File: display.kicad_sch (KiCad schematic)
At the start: 10 parts

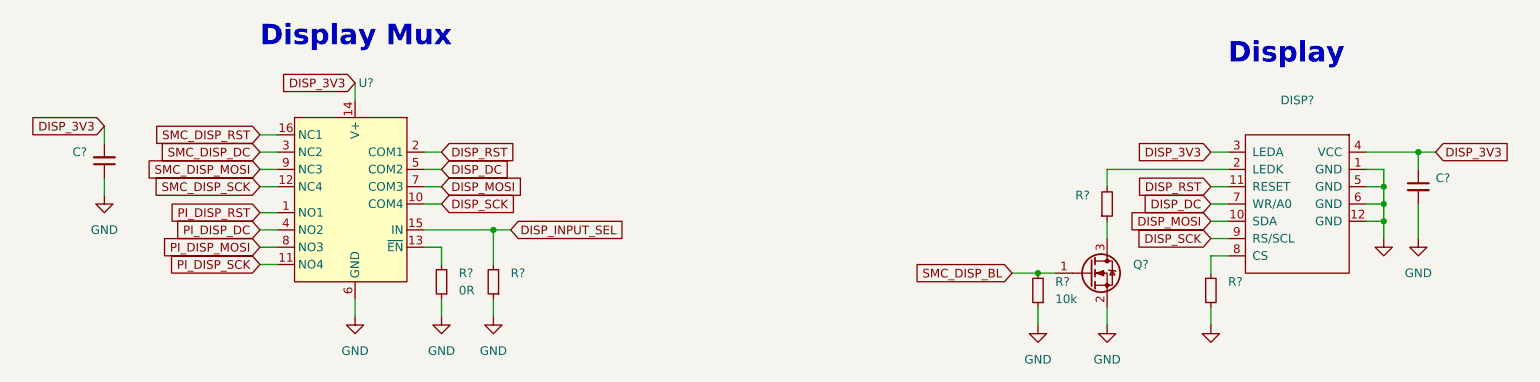
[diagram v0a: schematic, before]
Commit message: schem: first pass done, ERC passing
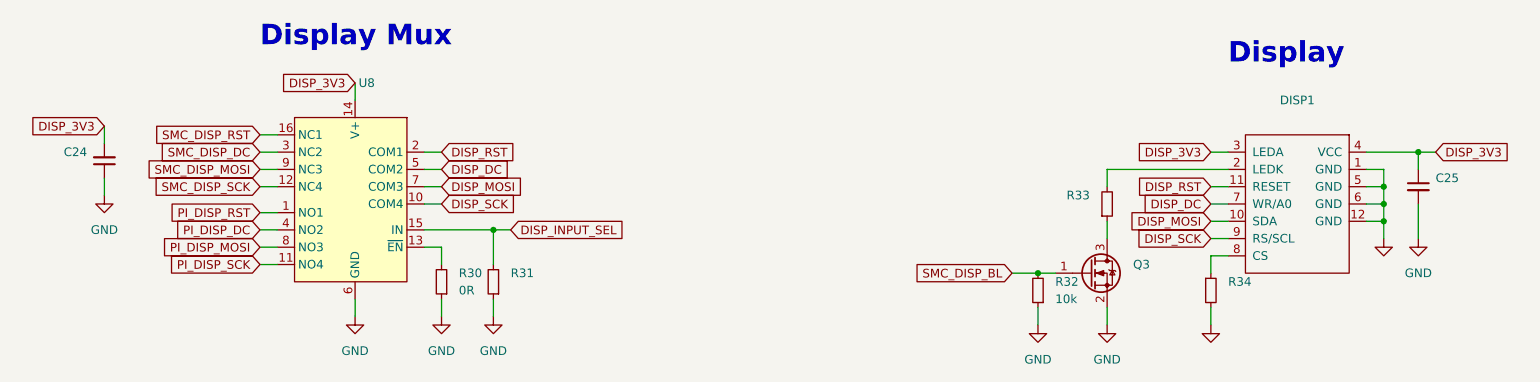
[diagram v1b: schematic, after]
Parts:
- Q3: renamed from Q?; footprint (none) -> Package_TO_SOT_SMD:SOT-23
- U8: renamed from U?; footprint (none) -> lcsc:UQFN-16_L2.6-W1.8-P0.40-BL
- gave numbers to parts that had none: 8
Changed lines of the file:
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@@
   (symbol (lib_id "lcsc:TS3A5018RSVR") (at 81.28 111.76 0) (mirror y) (unit 1)
     (in_bom yes) (on_board yes) (fields_autoplaced)
-    (property "Reference" "U?" (id 0) (at 81.8006 93.98 0)
+    (property "Reference" "U8" (id 0) (at 81.8006 93.98 0)
       (effects (font (size 1.27 1.27)) (justify right))
     )
@@
       (effects (font (size 1.27 1.27)) (justify right))
     )
-    (property "Footprint" "" (id 2) (at 81.28 135.89 0)
+    (property "Footprint" "lcsc:UQFN-16_L2.6-W1.8-P0.40-BL" (id 2) (at 81.28 135.89 0)
       (effects (font (size 1.27 1.27)) hide)
     )
@@
   (symbol (lib_id "power:GND") (at 237.49 116.84 0) (unit 1)
     (in_bom yes) (on_board yes) (fields_autoplaced)
-    (property "Reference" "#PWR?" (id 0) (at 237.49 123.19 0)
+    (property "Reference" "#PWR077" (id 0) (at 237.49 123.19 0)
       (effects (font (size 1.27 1.27)) hide)
     )
@@
   (symbol (lib_id "power:GND") (at 81.28 128.27 0) (unit 1)
     (in_bom yes) (on_board yes) (fields_autoplaced)
-    (property "Reference" "#PWR?" (id 0) (at 81.28 134.62 0)
+    (property "Reference" "#PWR070" (id 0) (at 81.28 134.62 0)
       (effects (font (size 1.27 1.27)) hide)
     )
@@
   (symbol (lib_id "Device:R_Small") (at 191.77 111.76 0) (mirror x) (unit 1)
     (in_bom yes) (on_board yes) (fields_autoplaced)
-    (property "Reference" "R?" (id 0) (at 189.23 110.4899 0)
+    (property "Reference" "R33" (id 0) (at 189.23 110.4899 0)
       (effects (font (size 1.27 1.27)) (justify right))
     )
@@
   (symbol (lib_id "Device:R_Small") (at 101.6 123.19 180) (unit 1)
     (in_bom yes) (on_board yes) (fields_autoplaced)
-    (property "Reference" "R?" (id 0) (at 104.14 121.9199 0)
+    (property "Reference" "R31" (id 0) (at 104.14 121.9199 0)
       (effects (font (size 1.27 1.27)) (justify right))
     )
@@
   (symbol (lib_id "power:GND") (at 191.77 129.54 0) (unit 1)
     (in_bom yes) (on_board yes) (fields_autoplaced)
-    (property "Reference" "#PWR?" (id 0) (at 191.77 135.89 0)
+    (property "Reference" "#PWR074" (id 0) (at 191.77 135.89 0)
       (effects (font (size 1.27 1.27)) hide)
     )
@@
   (symbol (lib_id "power:GND") (at 232.41 116.84 0) (unit 1)
     (in_bom yes) (on_board yes) (fields_autoplaced)
-    (property "Reference" "#PWR?" (id 0) (at 232.41 123.19 0)
+    (property "Reference" "#PWR076" (id 0) (at 232.41 123.19 0)
       (effects (font (size 1.27 1.27)) hide)
     )
@@
   (symbol (lib_id "power:GND") (at 207.01 129.54 0) (unit 1)
     (in_bom yes) (on_board yes) (fields_autoplaced)
-    (property "Reference" "#PWR?" (id 0) (at 207.01 135.89 0)
+    (property "Reference" "#PWR075" (id 0) (at 207.01 135.89 0)
       (effects (font (size 1.27 1.27)) hide)
     )
@@
   (symbol (lib_id "gigahawk:STP240320_0200B") (at 219.71 101.6 0) (mirror y) (unit 1)
     (in_bom yes) (on_board yes) (fields_autoplaced)
-    (property "Reference" "DISP?" (id 0) (at 219.71 96.52 0))
+    (property "Reference" "DISP1" (id 0) (at 219.71 96.52 0))
     (property "Value" "" (id 1) (at 219.71 99.06 0))
     (property "Footprint" "" (id 2) (at 219.71 101.6 0)
@@
   (symbol (lib_id "power:GND") (at 181.61 129.54 0) (unit 1)
     (in_bom yes) (on_board yes) (fields_autoplaced)
-    (property "Reference" "#PWR?" (id 0) (at 181.61 135.89 0)
+    (property "Reference" "#PWR073" (id 0) (at 181.61 135.89 0)
       (effects (font (size 1.27 1.27)) hide)
     )
@@
   (symbol (lib_id "Device:R_Small") (at 181.61 124.46 180) (unit 1)
     (in_bom yes) (on_board yes) (fields_autoplaced)
-    (property "Reference" "R?" (id 0) (at 184.15 123.1899 0)
+    (property "Reference" "R32" (id 0) (at 184.15 123.1899 0)
       (effects (font (size 1.27 1.27)) (justify right))
     )
@@
   (symbol (lib_id "power:GND") (at 93.98 128.27 0) (unit 1)
     (in_bom yes) (on_board yes) (fields_autoplaced)
-    (property "Reference" "#PWR?" (id 0) (at 93.98 134.62 0)
+    (property "Reference" "#PWR071" (id 0) (at 93.98 134.62 0)
       (effects (font (size 1.27 1.27)) hide)
     )
@@
   (symbol (lib_id "Device:R_Small") (at 207.01 124.46 0) (unit 1)
     (in_bom yes) (on_board yes) (fields_autoplaced)
-    (property "Reference" "R?" (id 0) (at 209.55 123.1899 0)
+    (property "Reference" "R34" (id 0) (at 209.55 123.1899 0)
       (effects (font (size 1.27 1.27)) (justify left))
     )
@@
   (symbol (lib_id "power:GND") (at 101.6 128.27 0) (unit 1)
     (in_bom yes) (on_board yes) (fields_autoplaced)
-    (property "Reference" "#PWR?" (id 0) (at 101.6 134.62 0)
+    (property "Reference" "#PWR072" (id 0) (at 101.6 134.62 0)
       (effects (font (size 1.27 1.27)) hide)
     )
@@
   (symbol (lib_id "Device:C_Small") (at 237.49 109.22 0) (unit 1)
     (in_bom yes) (on_board yes) (fields_autoplaced)
-    (property "Reference" "C?" (id 0) (at 240.03 107.9562 0)
+    (property "Reference" "C25" (id 0) (at 240.03 107.9562 0)
       (effects (font (size 1.27 1.27)) (justify left))
     )
@@
   (symbol (lib_id "Device:R_Small") (at 93.98 123.19 180) (unit 1)
     (in_bom yes) (on_board yes) (fields_autoplaced)
-    (property "Reference" "R?" (id 0) (at 96.52 121.9199 0)
+    (property "Reference" "R30" (id 0) (at 96.52 121.9199 0)
       (effects (font (size 1.27 1.27)) (justify right))
     )
@@
   (symbol (lib_id "Device:C_Small") (at 44.45 105.41 0) (mirror x) (unit 1)
     (in_bom yes) (on_board yes) (fields_autoplaced)
-    (property "Reference" "C?" (id 0) (at 41.91 104.1335 0)
+    (property "Reference" "C24" (id 0) (at 41.91 104.1335 0)
       (effects (font (size 1.27 1.27)) (justify right))
     )
@@
   (symbol (lib_id "Transistor_FET:BSS138") (at 189.23 121.92 0) (unit 1)
     (in_bom yes) (on_board yes) (fields_autoplaced)
-    (property "Reference" "Q?" (id 0) (at 195.58 120.6499 0)
+    (property "Reference" "Q3" (id 0) (at 195.58 120.6499 0)
       (effects (font (size 1.27 1.27)) (justify left))
     )
@@
       (effects (font (size 1.27 1.27)) (justify left))
     )
-    (property "Footprint" "" (id 2) (at 194.31 123.825 0)
+    (property "Footprint" "Package_TO_SOT_SMD:SOT-23" (id 2) (at 194.31 123.825 0)
       (effects (font (size 1.27 1.27) italic) (justify left) hide)
     )
@@
   (symbol (lib_id "power:GND") (at 44.45 110.49 0) (unit 1)
     (in_bom yes) (on_board yes) (fields_autoplaced)
-    (property "Reference" "#PWR?" (id 0) (at 44.45 116.84 0)
-      (effects (font (size 1.27 1.27)) hide)
-    )
+    (property "Reference" "#PWR069" (id 0) (at 44.45 116.84 0)
+      (effects (font (size 1.27 1.27)) hide)
+    )

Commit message: analysis: specify pi will be powered directly from VCC
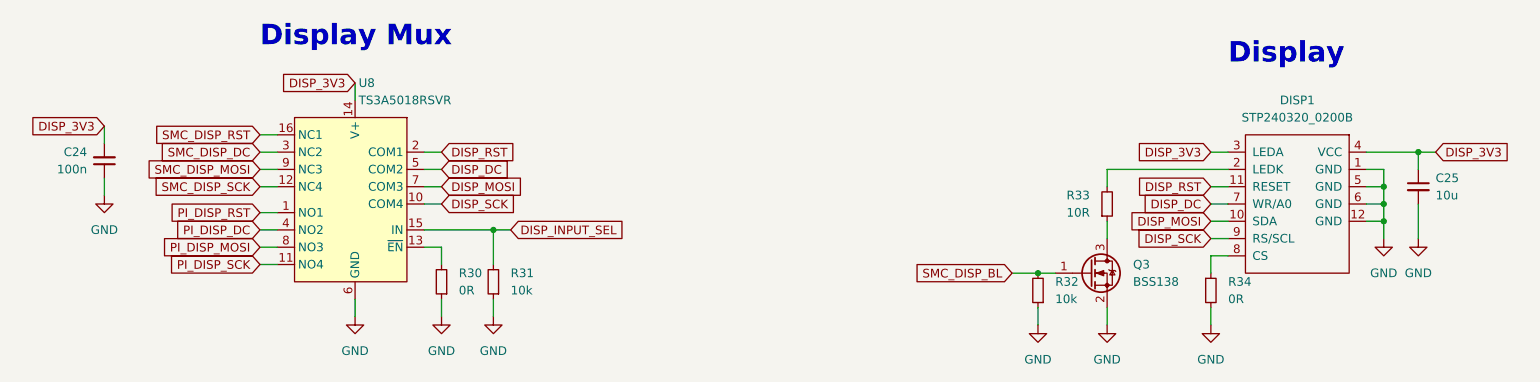
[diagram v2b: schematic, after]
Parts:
- C24: value (none) -> 100n; footprint (none) -> Capacitor_SMD:C_0402_1005Metric
- C25: value (none) -> 10u; footprint (none) -> Capacitor_SMD:C_0402_1005Metric
- DISP1: value (none) -> STP240320_0200B; footprint (none) -> Connector_Molex:Molex_SlimStack_54722-0164_2x08_P0.50mm_Vertical
- Q3: value (none) -> BSS138
- R30, R32: footprint (none) -> Resistor_SMD:R_0402_1005Metric
- R31: value (none) -> 10k; footprint (none) -> Resistor_SMD:R_0402_1005Metric
- R33: value (none) -> 10R; footprint (none) -> Resistor_SMD:R_0402_1005Metric
- R34: value (none) -> 0R; footprint (none) -> Resistor_SMD:R_0402_1005Metric
- U8: value (none) -> TS3A5018RSVR
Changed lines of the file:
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@@
       (effects (font (size 1.27 1.27)) (justify right))
     )
-    (property "Value" "" (id 1) (at 81.8006 96.52 0)
+    (property "Value" "TS3A5018RSVR" (id 1) (at 81.8006 96.52 0)
       (effects (font (size 1.27 1.27)) (justify right))
     )
@@
       (effects (font (size 1.27 1.27)) (justify right))
     )
-    (property "Value" "" (id 1) (at 189.23 113.0299 0)
-      (effects (font (size 1.27 1.27)) (justify right))
-    )
-    (property "Footprint" "" (id 2) (at 191.77 111.76 0)
+    (property "Value" "10R" (id 1) (at 189.23 113.0299 0)
+      (effects (font (size 1.27 1.27)) (justify right))
+    )
+    (property "Footprint" "Resistor_SMD:R_0402_1005Metric" (id 2) (at 191.77 111.76 0)
       (effects (font (size 1.27 1.27)) hide)
     )
@@
       (effects (font (size 1.27 1.27)) (justify right))
     )
-    (property "Value" "" (id 1) (at 104.14 124.4599 0)
-      (effects (font (size 1.27 1.27)) (justify right))
-    )
-    (property "Footprint" "" (id 2) (at 101.6 123.19 0)
+    (property "Value" "10k" (id 1) (at 104.14 124.4599 0)
+      (effects (font (size 1.27 1.27)) (justify right))
+    )
+    (property "Footprint" "Resistor_SMD:R_0402_1005Metric" (id 2) (at 101.6 123.19 0)
       (effects (font (size 1.27 1.27)) hide)
     )
@@
       (effects (font (size 1.27 1.27)) hide)
     )
-    (property "Value" "" (id 1) (at 232.41 121.92 0))
+    (property "Value" "GND" (id 1) (at 232.41 121.92 0))
     (property "Footprint" "" (id 2) (at 232.41 116.84 0)
       (effects (font (size 1.27 1.27)) hide)
@@
       (effects (font (size 1.27 1.27)) hide)
     )
-    (property "Value" "" (id 1) (at 207.01 134.62 0))
+    (property "Value" "GND" (id 1) (at 207.01 134.62 0))
     (property "Footprint" "" (id 2) (at 207.01 129.54 0)
       (effects (font (size 1.27 1.27)) hide)
@@
     (in_bom yes) (on_board yes) (fields_autoplaced)
     (property "Reference" "DISP1" (id 0) (at 219.71 96.52 0))
-    (property "Value" "" (id 1) (at 219.71 99.06 0))
-    (property "Footprint" "" (id 2) (at 219.71 101.6 0)
+    (property "Value" "STP240320_0200B" (id 1) (at 219.71 99.06 0))
+    (property "Footprint" "Connector_Molex:Molex_SlimStack_54722-0164_2x08_P0.50mm_Vertical" (id 2) (at 219.71 101.6 0)
       (effects (font (size 1.27 1.27)) hide)
     )
@@
       (effects (font (size 1.27 1.27)) (justify right))
     )
-    (property "Footprint" "" (id 2) (at 181.61 124.46 0)
+    (property "Footprint" "Resistor_SMD:R_0402_1005Metric" (id 2) (at 181.61 124.46 0)
       (effects (font (size 1.27 1.27)) hide)
     )
@@
       (effects (font (size 1.27 1.27)) (justify left))
     )
-    (property "Value" "" (id 1) (at 209.55 125.7299 0)
-      (effects (font (size 1.27 1.27)) (justify left))
-    )
-    (property "Footprint" "" (id 2) (at 207.01 124.46 0)
+    (property "Value" "0R" (id 1) (at 209.55 125.7299 0)
+      (effects (font (size 1.27 1.27)) (justify left))
+    )
+    (property "Footprint" "Resistor_SMD:R_0402_1005Metric" (id 2) (at 207.01 124.46 0)
       (effects (font (size 1.27 1.27)) hide)
     )
@@
       (effects (font (size 1.27 1.27)) (justify left))
     )
-    (property "Value" "" (id 1) (at 240.03 110.4962 0)
-      (effects (font (size 1.27 1.27)) (justify left))
-    )
-    (property "Footprint" "" (id 2) (at 237.49 109.22 0)
+    (property "Value" "10u" (id 1) (at 240.03 110.4962 0)
+      (effects (font (size 1.27 1.27)) (justify left))
+    )
+    (property "Footprint" "Capacitor_SMD:C_0402_1005Metric" (id 2) (at 237.49 109.22 0)
       (effects (font (size 1.27 1.27)) hide)
     )
@@
       (effects (font (size 1.27 1.27)) (justify right))
     )
-    (property "Footprint" "" (id 2) (at 93.98 123.19 0)
+    (property "Footprint" "Resistor_SMD:R_0402_1005Metric" (id 2) (at 93.98 123.19 0)
       (effects (font (size 1.27 1.27)) hide)
     )
@@
       (effects (font (size 1.27 1.27)) (justify right))
     )
-    (property "Value" "" (id 1) (at 41.91 106.6735 0)
-      (effects (font (size 1.27 1.27)) (justify right))
-    )
-    (property "Footprint" "" (id 2) (at 44.45 105.41 0)
+    (property "Value" "100n" (id 1) (at 41.91 106.6735 0)
+      (effects (font (size 1.27 1.27)) (justify right))
+    )
+    (property "Footprint" "Capacitor_SMD:C_0402_1005Metric" (id 2) (at 44.45 105.41 0)
       (effects (font (size 1.27 1.27)) hide)
     )
@@
       (effects (font (size 1.27 1.27)) (justify left))
     )
-    (property "Value" "" (id 1) (at 195.58 123.1899 0)
-      (effects (font (size 1.27 1.27)) (justify left))
-    )
+    (property "Value" "BSS138" (id 1) (at 195.58 123.1899 0)
+      (effects (font (size 1.27 1.27)) (justify left))
+    )

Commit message: schem: migrate away from LCSC exclusive parts
- layout: migrate away from lcsc footprints
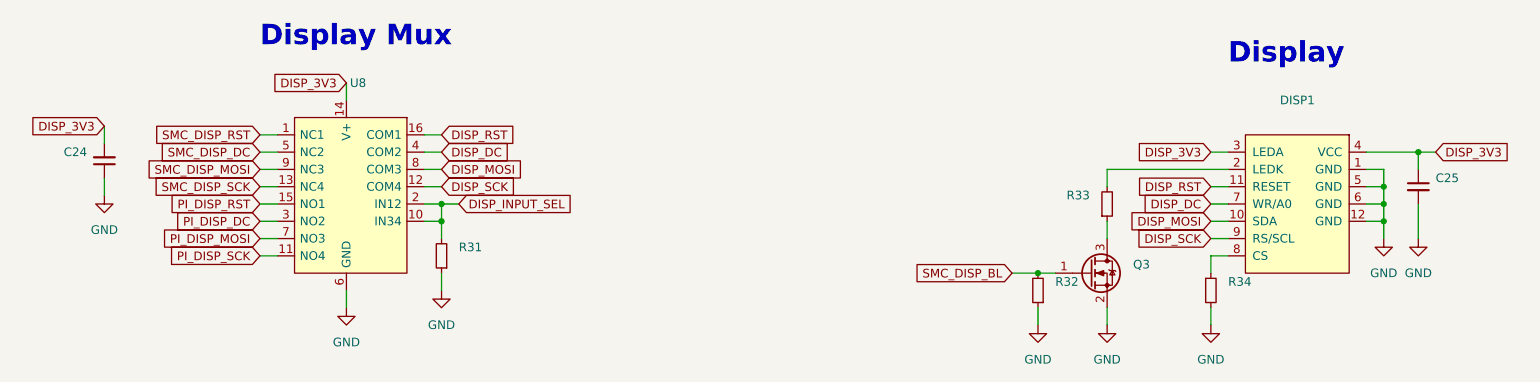
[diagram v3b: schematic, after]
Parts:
- removed R30: 0R, Resistor_SMD:R_0402_1005Metric, symbol Device:R_Small
- removed U8: TS3A5018RSVR, lcsc:UQFN-16_L2.6-W1.8-P0.40-BL, symbol lcsc:TS3A5018RSVR
- added U8: (no value), symbol gigahawk:RS2299XTQC16
- C24: value 100n -> (none); footprint Capacitor_SMD:C_0402_1005Metric -> (none)
- C25: value 10u -> (none); footprint Capacitor_SMD:C_0402_1005Metric -> (none)
- DISP1: value STP240320_0200B -> (none); footprint Connector_Molex:Molex_SlimStack_54722-0164_2x08_P0.50mm_Vertical -> (none); Digikey Part (none) -> WM3446TR-ND; Digikey Price/Stock (none) -> https://www.digikey.ca/en/products/detail/molex/0547220164/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; LCSC Part (none) -> C564081; Manufacturer (none) -> MOLEX; Manufacturer Part (none) -> 54722-0164; Mouser Part (none) -> 538-54722-0164; Mouser Price/Stock (none) -> https://www.mouser.ca/ProductDetail/Molex/54722-0164?qs=OdN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
- Q3: value BSS138 -> (none); footprint Package_TO_SOT_SMD:SOT-23 -> (none); Digikey Part (none) -> BSS138TR-ND; Digikey Price/Stock (none) -> https://www.digikey.com/en/products/detail/onsemi/BSS138/24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; JLC Part (none) -> Extended Part; LCSC Part (none) -> C52895; Manufacturer (none) -> onsemi; Manufacturer Part (none) -> BSS138; Mouser Part (none) -> 512-BSS138; Mouser Price/Stock (none) -> https://www.mouser.ca/ProductDetail/onsemi-Fairchild/BSS138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
- R31, R32: value 10k -> (none); footprint Resistor_SMD:R_0402_1005Metric -> (none)
- R33: value 10R -> (none); footprint Resistor_SMD:R_0402_1005Metric -> (none)
- R34: value 0R -> (none); footprint Resistor_SMD:R_0402_1005Metric -> (none)
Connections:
- net DISP_3V3: now also U8.14 (V+)
- net DISP_DC: now also U8.4 (COM2)
- net DISP_INPUT_SEL: now also U8.10 (IN34), U8.2 (IN12)
- net DISP_MOSI: now also U8.8 (COM3)
- net DISP_RST: now also U8.16 (COM1)
- net DISP_SCK: now also U8.12 (COM4)
- net GND: now also U8.6 (GND)
- net PI_DISP_DC: now also U8.3 (NO2)
- net PI_DISP_MOSI: now also U8.7 (NO3)
- net PI_DISP_RST: now also U8.15 (NO1)
- net PI_DISP_SCK: now also U8.11 (NO4)
- net SMC_DISP_DC: now also U8.5 (NC2)
- net SMC_DISP_MOSI: now also U8.9 (NC3)
- net SMC_DISP_RST: now also U8.1 (NC1)
- net SMC_DISP_SCK: now also U8.13 (NC4)
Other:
- moved on the sheet: R31
